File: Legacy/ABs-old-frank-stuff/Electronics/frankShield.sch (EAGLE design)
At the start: 27 parts, among them IC1 BD6230F, IC2 BD6230F, IC3 TS5A23157

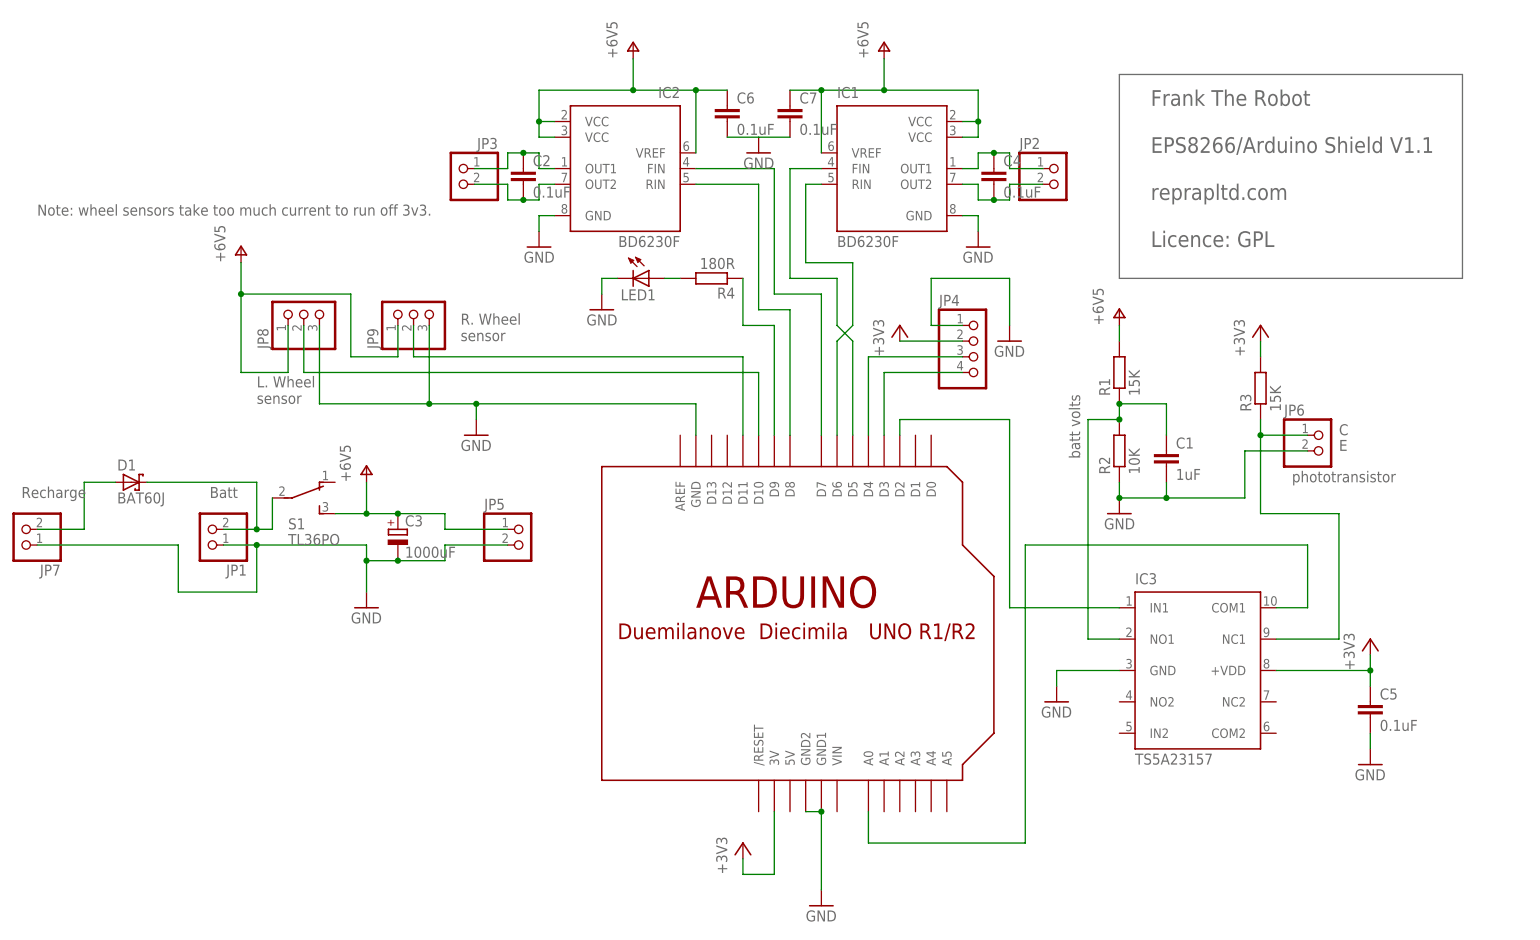
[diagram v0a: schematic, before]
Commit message: PCBs corrected (D9 now LED) and improved (wheel sensor has 4 mounting holes); software updated to match.
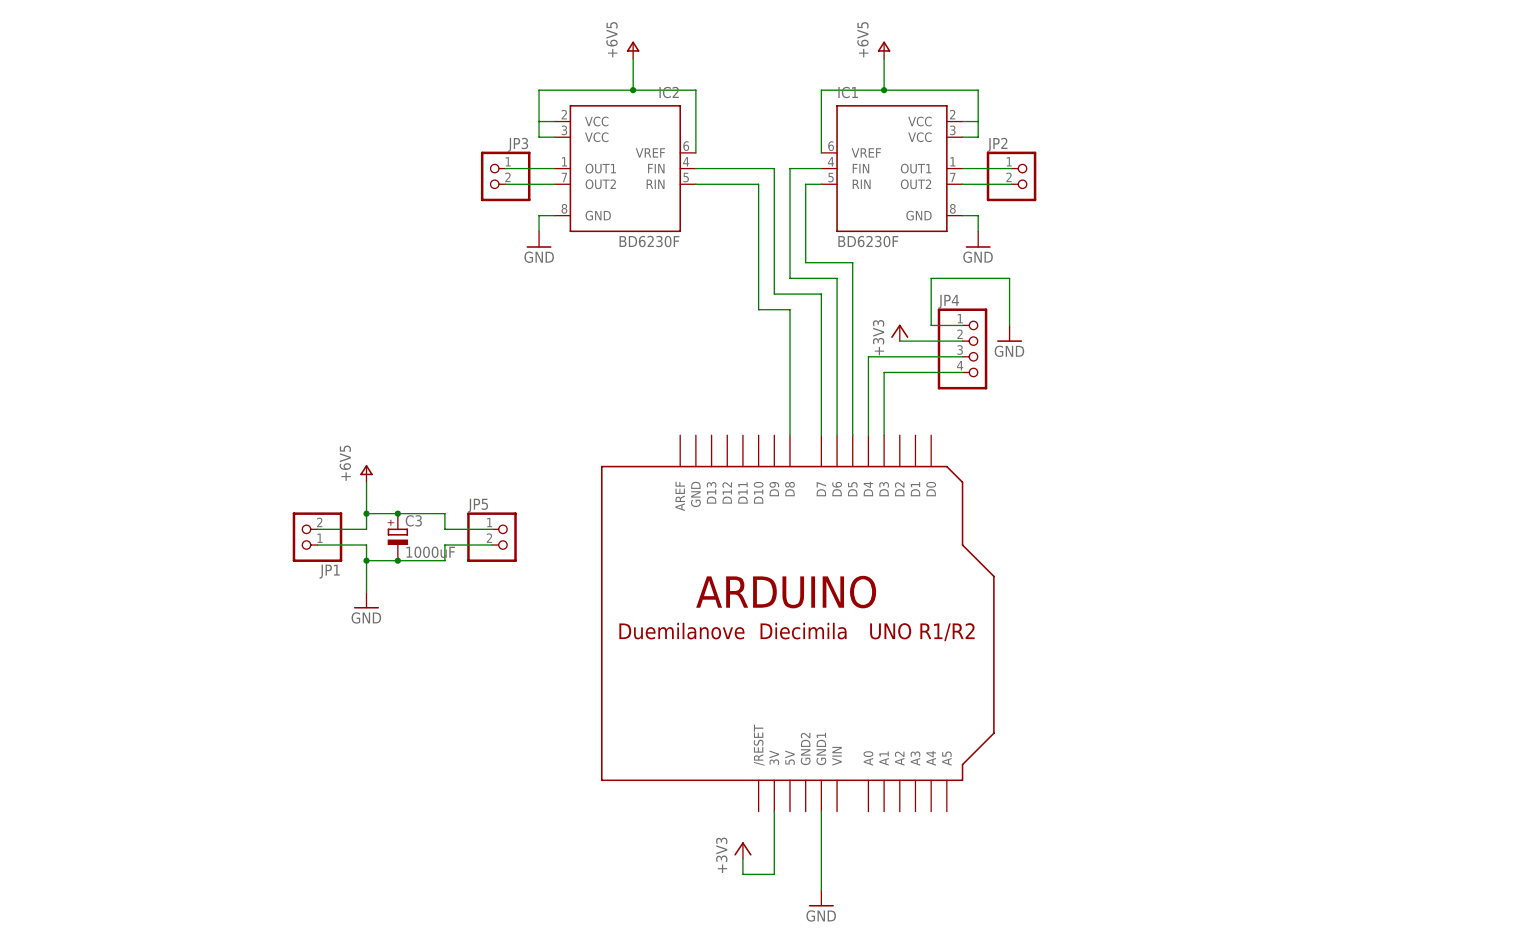
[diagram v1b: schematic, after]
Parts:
- removed C1: 1uF, rcl:C-EUC0805
- removed C2, C4, C5, C6, C7: 0.1uF, rcl:C-EUC0805
- removed D1: BAT60J, diode:BAT60J
- removed IC3: TS5A23157, reprapltd:TS5A23157
- removed JP6, JP7: (no value), pinhead:PINHD-1X2
- removed JP8, JP9: (no value), pinhead:PINHD-1X3
- removed LED1: (no value), led:LEDCHIP-LED0805
- removed R1, R3: 15K, rcl:R-EU_M0805
- removed R2: 10K, rcl:R-EU_M0805
- removed R4: 180R, rcl:R-EU_M0805
- removed S1: TL36PO, switch:TL36PO
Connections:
- removed net N$11: IC3.COM1, U$1.A0
- removed net N$12: C1.1, IC3.NO1, R1.1, R2.2
- removed net N$13: D1.C, JP1.2, S1.P
- removed net N$14: IC3.NC1, JP6.1, R3.1
- removed net N$15: IC3.IN1, U$1.D2
- removed net N$16: D1.A, JP7.2
- removed net N$17: JP9.2, U$1.D11
- removed net N$18: JP8.2, U$1.D10
- removed net N$19: LED1.A, R4.2
- removed net N$20: R4.1, U$1.D9
- net +3V3: no longer C5.1, IC3.+VDD, R3.2
- net GND: no longer C1.2, C5.2, C6.2, C7.2, IC3.GND, JP6.2, JP7.1, JP8.3, JP9.3, LED1.C, R2.1, U$1.GND, U$1.GND2
- net N$3: now also IC1.OUT1, JP2.1; no longer C2.1, IC2.OUT1, JP3.1
- net N$4: now also IC1.OUT2, JP2.2; no longer C2.2, IC2.OUT2, JP3.2
- net N$5: now also IC2.OUT1, JP3.1; no longer C4.1, IC1.OUT1, JP2.1
- net N$6: now also IC2.OUT2, JP3.2; no longer C4.2, IC1.OUT2, JP2.2
- net N$7: now also U$1.D5; no longer U$1.D6
- net N$8: now also U$1.D6; no longer U$1.D5
- net V+: now also JP1.2; no longer C6.1, C7.1, JP8.1, JP9.1, R1.2, S1.S
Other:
- note removed: "Batt"
- note removed: "C"
- note removed: "E"
- note removed: "Frank The Robot EPS8266/Arduino Shield V1.1 reprapltd.com Licence: GPL"
- note removed: "L. Wheel sensor"
- note removed: "LIDAR"
- note removed: "Left Motor"
- note removed: "Note: wheel sensors take too much current to run off 3v3."
- note removed: "Power In"
- note removed: "Power To Arduino"
- note removed: "R. Wheel sensor"
- note removed: "Recharge"
- note removed: "Right Motor"
- note removed: "batt volts"
- note removed: "phototransistor"
- moved on the sheet: JP1, JP2, JP3, JP5
